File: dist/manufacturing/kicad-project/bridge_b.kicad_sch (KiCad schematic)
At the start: 18 parts, among them Q10 CSD19534Q5A, Q11 CSD19534Q5A, Q12 CSD19534Q5A, Q13 CSD19534Q5A

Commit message: Complete orderable PD1180-EPR board release
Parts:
- removed Q10, Q11, Q12, Q13: CSD19534Q5A, symbol Device:U_CSD19534Q5A
- removed RS2: HoLLR2512-3W-33mR-1%, symbol Device:U_HoLLR2512-3W-33mR-1
- removed VMOTOR (x4): VMOTOR, symbol Custom:rail_up
- added Q10: Q10, symbol Custom:CSD19534Q5A_POWER_NMOS
- added Q11: Q11, symbol Custom:CSD19534Q5A_POWER_NMOS
- added Q12: Q12, symbol Custom:CSD19534Q5A_POWER_NMOS
- added Q13: Q13, symbol Custom:CSD19534Q5A_POWER_NMOS
- added R110: 33mΩ, symbol Device:boxresistor_down
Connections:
- net at R50.2: now also Q12.4 (gate); no longer R52.1
- net at GND.1: now also R110.2
- net at R47.2: now also Q11.4 (gate); no longer R49.1
- net at R51.2: now also Q13.4 (gate); no longer R53.1
- net at R46.2: now also Q10.4 (gate); no longer R48.1
- net at R52.2: now also Q12.1 (source), Q12.2 (S2), Q12.3 (S3)
- new net: Q11.5 (drain), Q11.6 (D2), Q11.7 (D3), Q11.8 (D4), Q11.9 (D5)
- new net: Q13.5 (drain), Q13.6 (D2), Q13.7 (D3), Q13.8 (D4), Q13.9 (D5)
- new net: Q10.5 (drain), Q10.6 (D2), Q10.7 (D3), Q10.8 (D4), Q10.9 (D5)
- new net: Q12.5 (drain), Q12.6 (D2), Q12.7 (D3), Q12.8 (D4), Q12.9 (D5)
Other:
- note added: "Q10/Q12: high-side MOSFETs. Q11/Q13: low-side MOSFETs. R110: 33 mOhm, 3 W phase-current shunt."

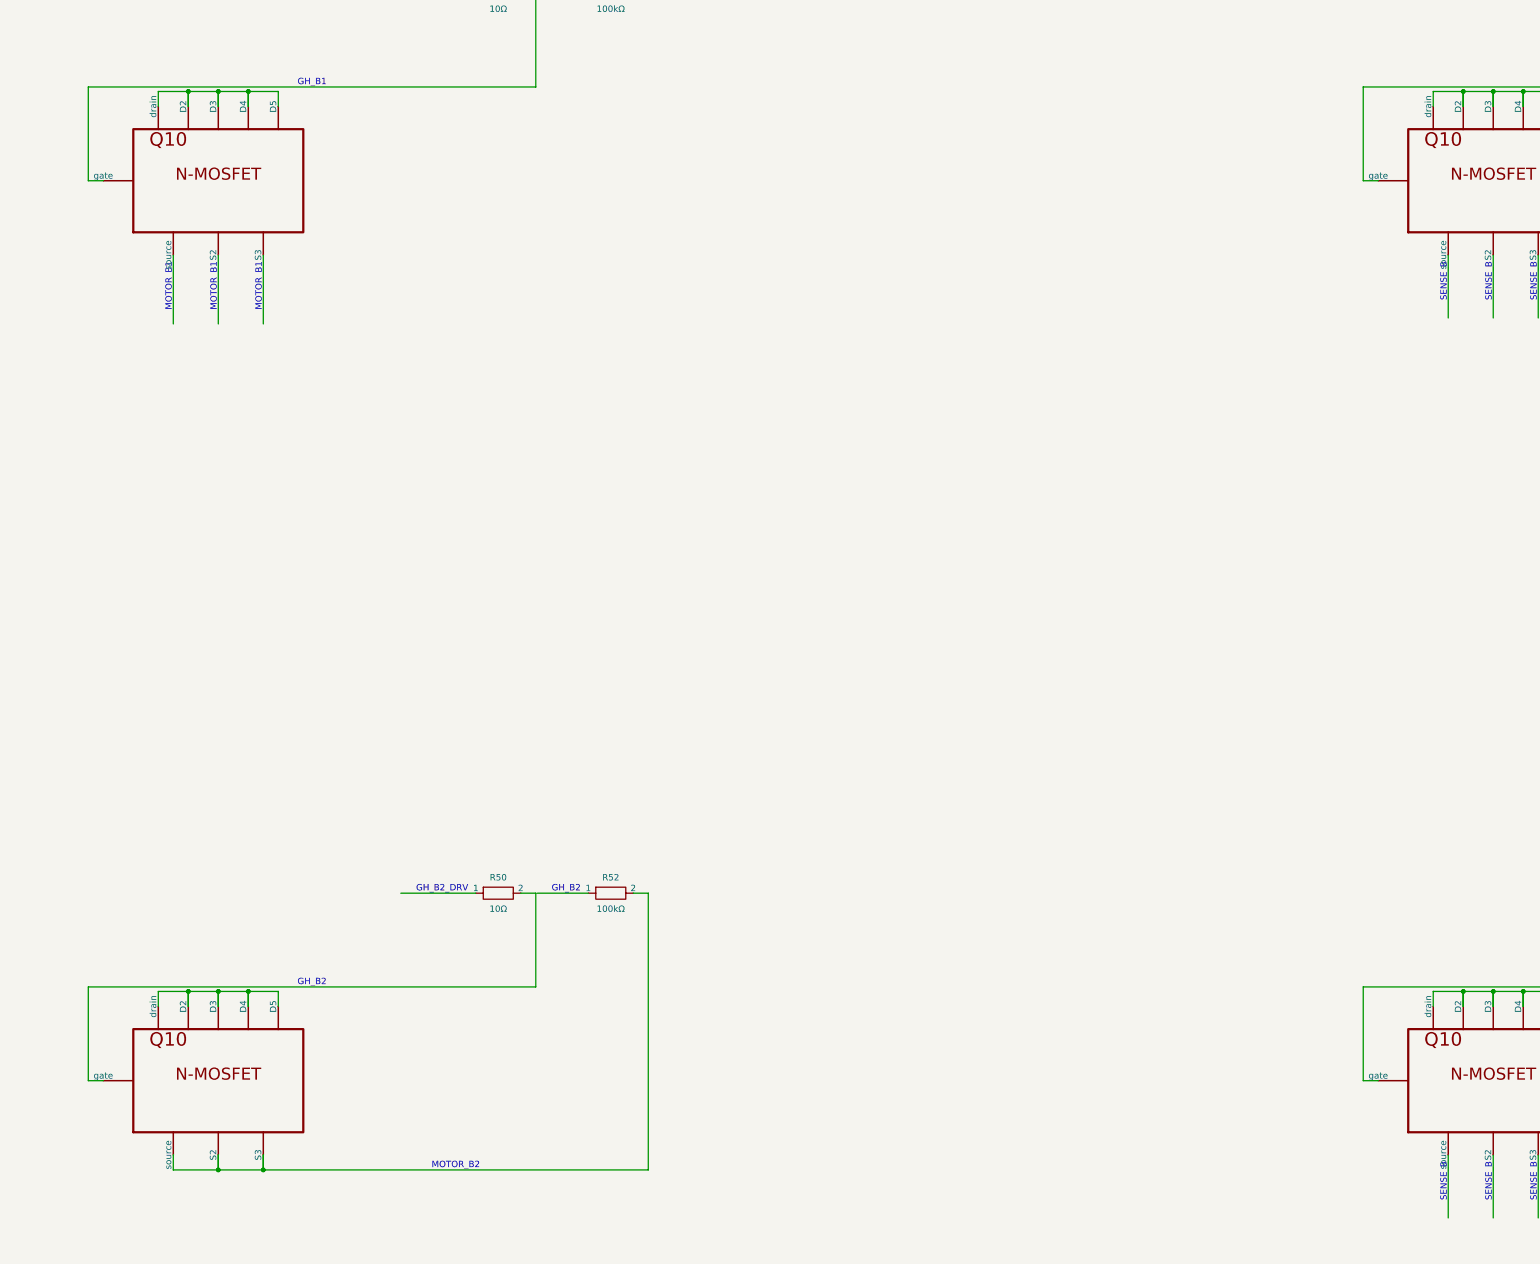
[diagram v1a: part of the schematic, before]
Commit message: Fix schematic style and top-side reset switch
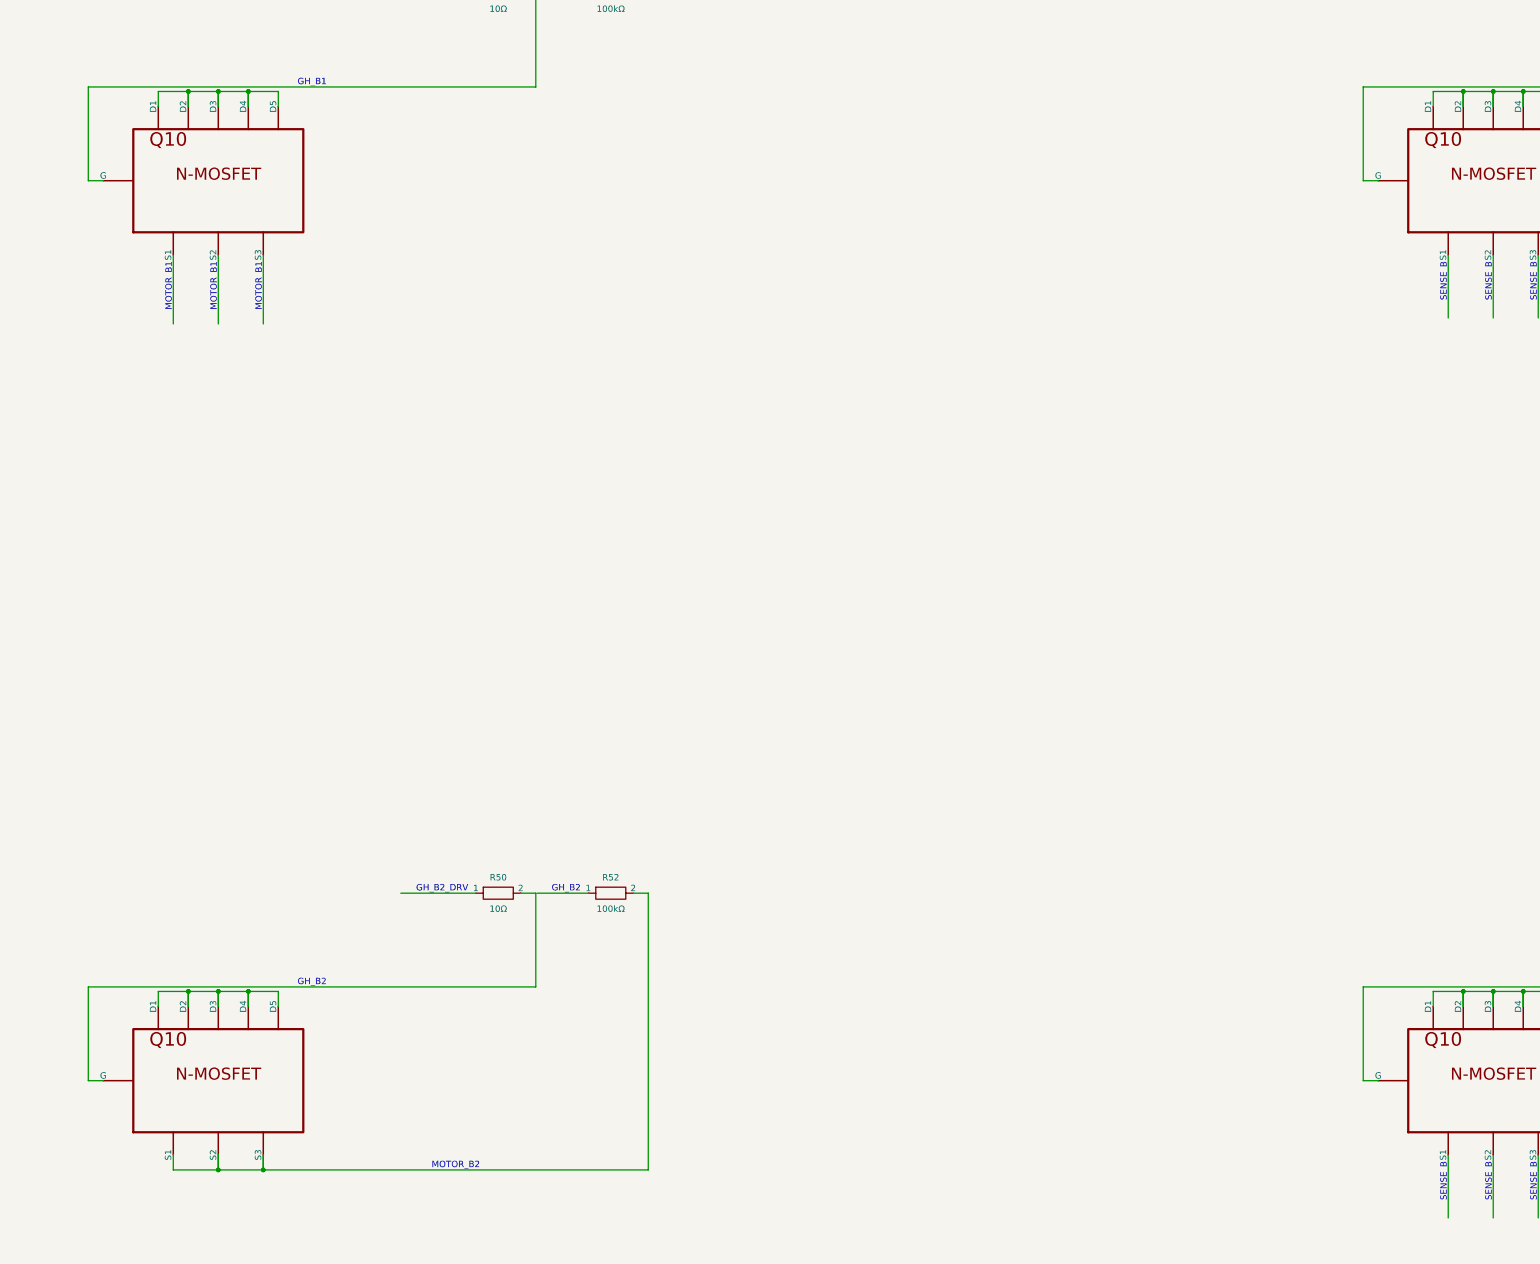
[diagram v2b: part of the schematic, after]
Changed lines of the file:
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@@
     (instances
       (project ""
-        (path "/f5f6ca0d-0209-4855-99b3-5a1edaa43ca4/eb2cc6d8-a710-4993-8b83-adfaae8e2747"
+        (path "/17a83a49-7a29-40ba-a4d1-006f579ceb16/48b7c8ff-39d1-4978-9cdb-f60ac64b3a8d"
           (reference "Q10")
           (unit 1)
@@
     (instances
       (project ""
-        (path "/f5f6ca0d-0209-4855-99b3-5a1edaa43ca4/eb2cc6d8-a710-4993-8b83-adfaae8e2747"
+        (path "/17a83a49-7a29-40ba-a4d1-006f579ceb16/48b7c8ff-39d1-4978-9cdb-f60ac64b3a8d"
           (reference "Q11")
           (unit 1)
@@
     (instances
       (project ""
-        (path "/f5f6ca0d-0209-4855-99b3-5a1edaa43ca4/eb2cc6d8-a710-4993-8b83-adfaae8e2747"
+        (path "/17a83a49-7a29-40ba-a4d1-006f579ceb16/48b7c8ff-39d1-4978-9cdb-f60ac64b3a8d"
           (reference "R46")
           (unit 1)
@@
     (instances
       (project ""
-        (path "/f5f6ca0d-0209-4855-99b3-5a1edaa43ca4/eb2cc6d8-a710-4993-8b83-adfaae8e2747"
+        (path "/17a83a49-7a29-40ba-a4d1-006f579ceb16/48b7c8ff-39d1-4978-9cdb-f60ac64b3a8d"
           (reference "R47")
           (unit 1)
@@
     (instances
       (project ""
-        (path "/f5f6ca0d-0209-4855-99b3-5a1edaa43ca4/eb2cc6d8-a710-4993-8b83-adfaae8e2747"
+        (path "/17a83a49-7a29-40ba-a4d1-006f579ceb16/48b7c8ff-39d1-4978-9cdb-f60ac64b3a8d"
           (reference "R48")
           (unit 1)
@@
     (instances
       (project ""
-        (path "/f5f6ca0d-0209-4855-99b3-5a1edaa43ca4/eb2cc6d8-a710-4993-8b83-adfaae8e2747"
+        (path "/17a83a49-7a29-40ba-a4d1-006f579ceb16/48b7c8ff-39d1-4978-9cdb-f60ac64b3a8d"
           (reference "R49")
           (unit 1)
@@
     (instances
       (project ""
-        (path "/f5f6ca0d-0209-4855-99b3-5a1edaa43ca4/eb2cc6d8-a710-4993-8b83-adfaae8e2747"
+        (path "/17a83a49-7a29-40ba-a4d1-006f579ceb16/48b7c8ff-39d1-4978-9cdb-f60ac64b3a8d"
           (reference "Q12")
           (unit 1)
@@
     (instances
       (project ""
-        (path "/f5f6ca0d-0209-4855-99b3-5a1edaa43ca4/eb2cc6d8-a710-4993-8b83-adfaae8e2747"
+        (path "/17a83a49-7a29-40ba-a4d1-006f579ceb16/48b7c8ff-39d1-4978-9cdb-f60ac64b3a8d"
           (reference "Q13")
           (unit 1)
@@
     (instances
       (project ""
-        (path "/f5f6ca0d-0209-4855-99b3-5a1edaa43ca4/eb2cc6d8-a710-4993-8b83-adfaae8e2747"
+        (path "/17a83a49-7a29-40ba-a4d1-006f579ceb16/48b7c8ff-39d1-4978-9cdb-f60ac64b3a8d"
           (reference "R50")
           (unit 1)
@@
     (instances
       (project ""
-        (path "/f5f6ca0d-0209-4855-99b3-5a1edaa43ca4/eb2cc6d8-a710-4993-8b83-adfaae8e2747"
+        (path "/17a83a49-7a29-40ba-a4d1-006f579ceb16/48b7c8ff-39d1-4978-9cdb-f60ac64b3a8d"
           (reference "R51")
           (unit 1)
@@
     (instances
       (project ""
-        (path "/f5f6ca0d-0209-4855-99b3-5a1edaa43ca4/eb2cc6d8-a710-4993-8b83-adfaae8e2747"
+        (path "/17a83a49-7a29-40ba-a4d1-006f579ceb16/48b7c8ff-39d1-4978-9cdb-f60ac64b3a8d"
           (reference "R52")
           (unit 1)
@@
     (instances
       (project ""
-        (path "/f5f6ca0d-0209-4855-99b3-5a1edaa43ca4/eb2cc6d8-a710-4993-8b83-adfaae8e2747"
+        (path "/17a83a49-7a29-40ba-a4d1-006f579ceb16/48b7c8ff-39d1-4978-9cdb-f60ac64b3a8d"
           (reference "R53")
           (unit 1)
@@
     (instances
       (project ""
-        (path "/f5f6ca0d-0209-4855-99b3-5a1edaa43ca4/eb2cc6d8-a710-4993-8b83-adfaae8e2747"
+        (path "/17a83a49-7a29-40ba-a4d1-006f579ceb16/48b7c8ff-39d1-4978-9cdb-f60ac64b3a8d"
           (reference "R110")
           (unit 1)
@@
     (instances
       (project ""
-        (path "/f5f6ca0d-0209-4855-99b3-5a1edaa43ca4/eb2cc6d8-a710-4993-8b83-adfaae8e2747"
+        (path "/17a83a49-7a29-40ba-a4d1-006f579ceb16/48b7c8ff-39d1-4978-9cdb-f60ac64b3a8d"
           (reference "GND")
           (unit 1)

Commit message: fix: finalize single-port EPR controller
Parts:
- removed GND: GND, symbol Custom:rail_down
- Q10, Q11, Q12, Q13: footprint (none) -> CSD19534Q5A
- R110: footprint (none) -> HoLLR2512-3W-33mR-1
- R46, R47, R48, R49, R50, R51, R52, R53: footprint (none) -> resistor_res0603
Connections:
- net GL_B2_DRV: now reaches R51.1
- net GL_B2: now reaches Q13.4 (G), R51.2
- net GL_B2: now also R53.1
- net SENSE_B: now reaches R110.1
- net SENSE_B: now also Q11.1 (S1), Q11.2 (S2), Q11.3 (S3), Q13.1 (S1), Q13.2 (S2), Q13.3 (S3), R49.2, R53.2
- net GND: now reaches R110.2
- net GL_B1: now reaches R49.1
- net GL_B1: now also Q11.4 (G), R47.2
- net MOTOR_B1: now reaches Q11.5 (D1), Q11.6 (D2), Q11.7 (D3), Q11.8 (D4), Q11.9 (D5)
- net MOTOR_B1: now also Q10.1 (S1), Q10.2 (S2), Q10.3 (S3), R48.2
- net GH_B2: now reaches R52.1
- net GH_B2: now also Q12.4 (G), R50.2
- net MOTOR_B2: now reaches Q12.1 (S1), Q12.2 (S2), Q12.3 (S3), R52.2
- net MOTOR_B2: now also Q13.5 (D1), Q13.6 (D2), Q13.7 (D3), Q13.8 (D4), Q13.9 (D5)
- net GH_B2_DRV: now reaches R50.1
- net GH_B1: now reaches R48.1
- net GH_B1: now also Q10.4 (G), R46.2
- net VMOTOR: now reaches Q12.5 (D1), Q12.6 (D2), Q12.7 (D3), Q12.8 (D4), Q12.9 (D5)
- net VMOTOR: now also Q10.5 (D1), Q10.6 (D2), Q10.7 (D3), Q10.8 (D4), Q10.9 (D5)
- net GH_B1_DRV: now reaches R46.1
- net GL_B1_DRV: now reaches R47.1

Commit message: Implement dual USB power/data ECO and consolidate industrial I/O
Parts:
- removed Q10: Q10, CSD19534Q5A, symbol Custom:CSD19534Q5A_POWER_NMOS
- removed Q11: Q11, CSD19534Q5A, symbol Custom:CSD19534Q5A_POWER_NMOS
- removed Q12: Q12, CSD19534Q5A, symbol Custom:CSD19534Q5A_POWER_NMOS
- removed Q13: Q13, CSD19534Q5A, symbol Custom:CSD19534Q5A_POWER_NMOS
- added Q10, Q11, Q12, Q13: CSD19534Q5A, CSD19534Q5A, symbol Device:U_CSD19534Q5A
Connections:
- net GH_B1: now also Q10.4 (G)
- net GH_B2: now also Q12.4 (G)
- net GL_B1: now also Q11.4 (G)
- net GL_B2: now also Q13.4 (G)
- net MOTOR_B1: now also Q10.1 (S1), Q10.2 (S2), Q10.3 (S3), Q11.5 (D1), Q11.6 (D2), Q11.7 (D3), Q11.8 (D4), Q11.9 (D5)
- net MOTOR_B2: now also Q12.1 (S1), Q12.2 (S2), Q12.3 (S3), Q13.5 (D1), Q13.6 (D2), Q13.7 (D3), Q13.8 (D4), Q13.9 (D5)
- net SENSE_B: now also Q11.1 (S1), Q11.2 (S2), Q11.3 (S3), Q13.1 (S1), Q13.2 (S2), Q13.3 (S3)
- net VMOTOR: now also Q10.5 (D1), Q10.6 (D2), Q10.7 (D3), Q10.8 (D4), Q10.9 (D5), Q12.5 (D1), Q12.6 (D2), Q12.7 (D3), Q12.8 (D4), Q12.9 (D5)
